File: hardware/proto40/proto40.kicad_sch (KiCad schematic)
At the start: 0 parts

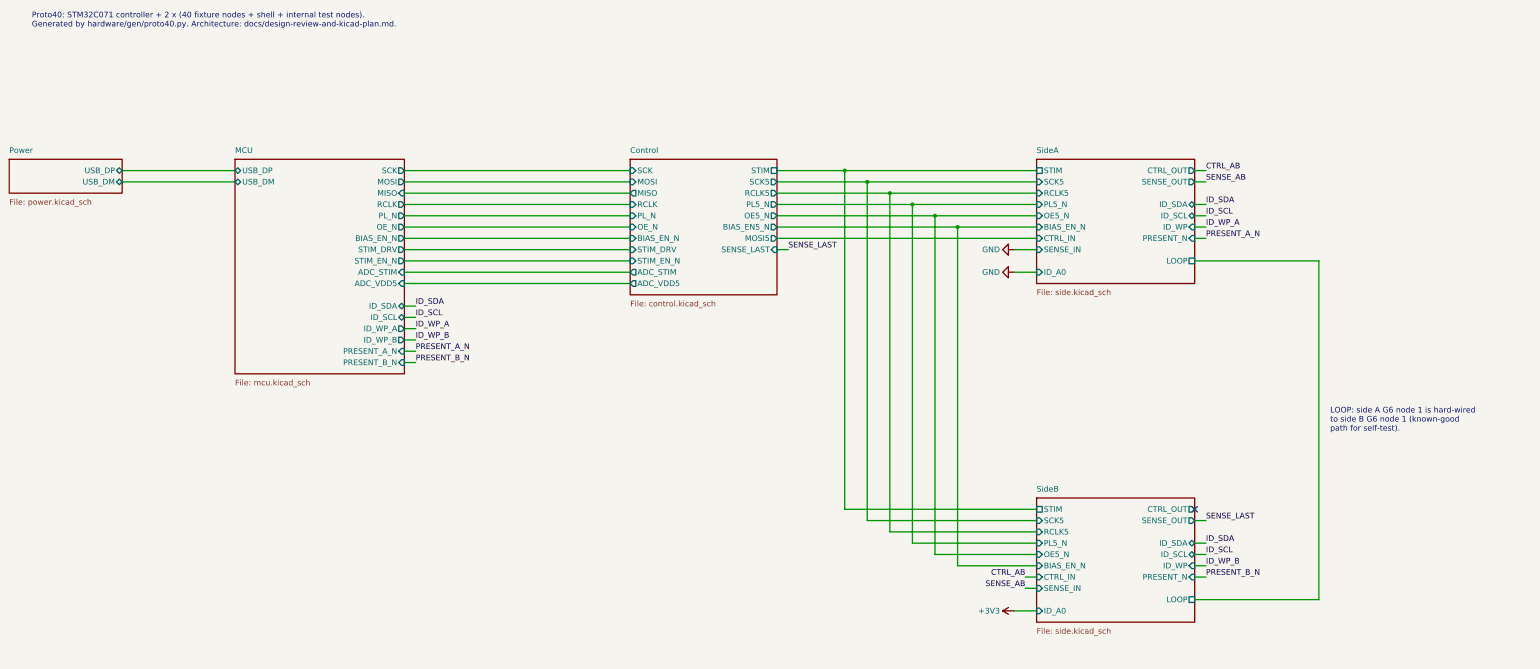
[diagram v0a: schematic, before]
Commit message: Resolve Proto40 house-style review findings
- Fixture ID lines: TVS at the connector plus series R on SDA/SCL/WP/A0/PRESENT_N;
  ID_VCC limited by 100 ohm 1206 (D14). PRESENT_N pull-up moved to MCU side.
- Shunt clamp ballast R104 is 6.8 ohm 2512, BCP53 copper note (D15).
- MPN/Manufacturer on every part (generic Yageo/Samsung passives), LCSC TBD.
- Test points on the '595 outputs and chain in/out; pull-downs on SCK/RCLK.
- Root sheet: CTRL/SENSE chains and ID lines drawn as wires; ASCII-only text.
- layoutcheck: non-ASCII, title length, text/text gap, text/wire clearance,
  NC flag on wired pin; wider char estimate. CI ERC runs --severity-all.
- Netclass patterns tightened for STIM/MUX and SPI nets.

Co-Authored-By: Claude Opus 5.5 (1M context) <noreply@anthropic.com>
Claude-Session: https://claude.ai/code/session_013SDanWEFU4wFXEYfZ6C9GH
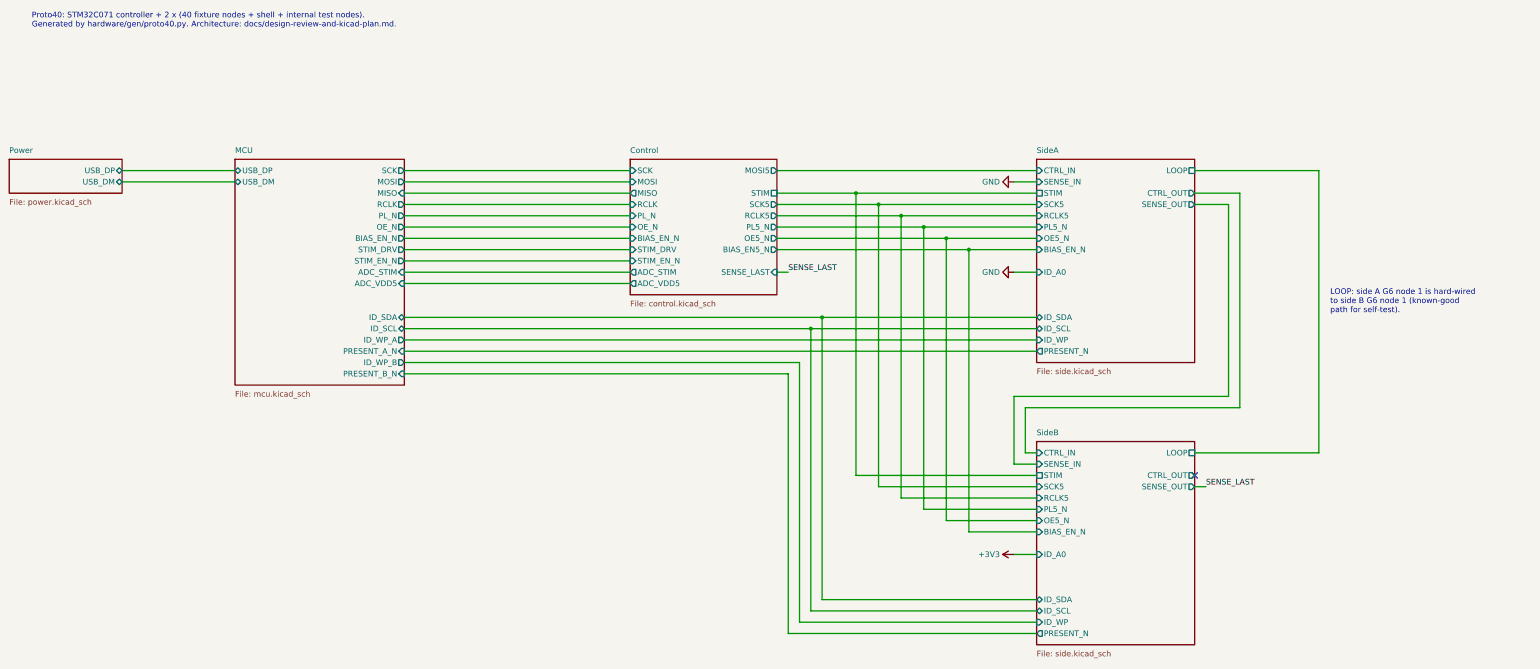
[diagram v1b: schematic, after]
